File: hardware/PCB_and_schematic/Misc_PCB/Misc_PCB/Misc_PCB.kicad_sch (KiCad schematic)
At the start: 0 parts

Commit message: add misc board schematic
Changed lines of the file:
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@@
 	)
 	(sheet
-		(at 18.796 59.944)
-		(size 55.626 36.576)
+		(at 18.796 64.389)
+		(size 44.069 27.686)
 		(fields_autoplaced yes)
 		(stroke
@@
 		)
 		(property "Sheetname" "SD Card Switcher"
-			(at 18.796 59.2324 0)
+			(at 18.796 63.3124 0)
 			(effects
 				(font
-					(size 1.27 1.27)
+					(size 2 2)
+					(bold yes)
 				)
 				(justify left bottom)
@@
 		)
 		(property "Sheetfile" "schematics/sd_card_switcher_sch.kicad_sch"
-			(at 18.796 97.1046 0)
+			(at 18.796 92.6596 0)
 			(effects
 				(font

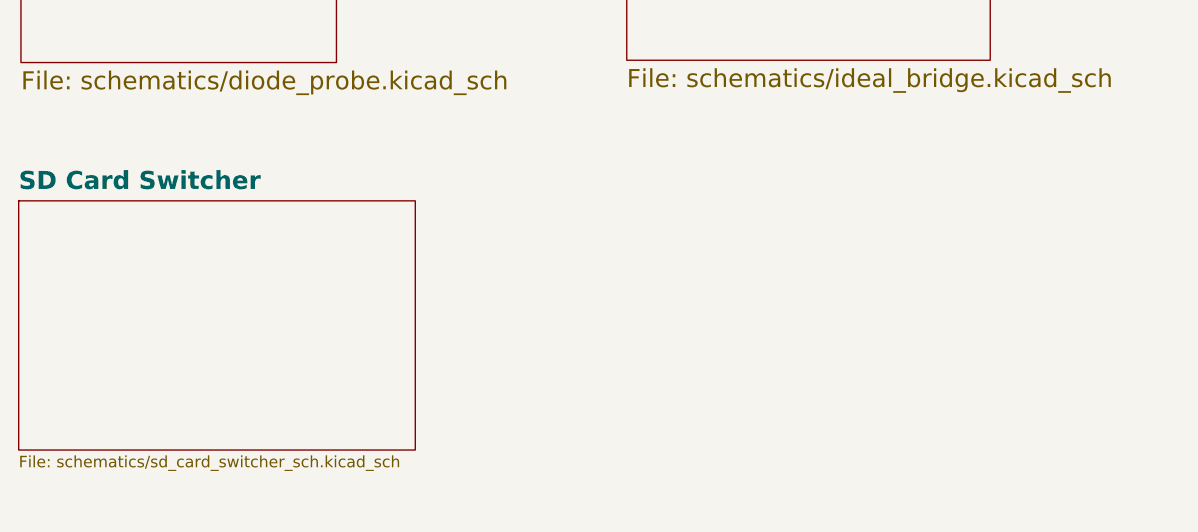
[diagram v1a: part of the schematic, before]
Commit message: Add SD card switcher circuit, some changes in pcb and schematic
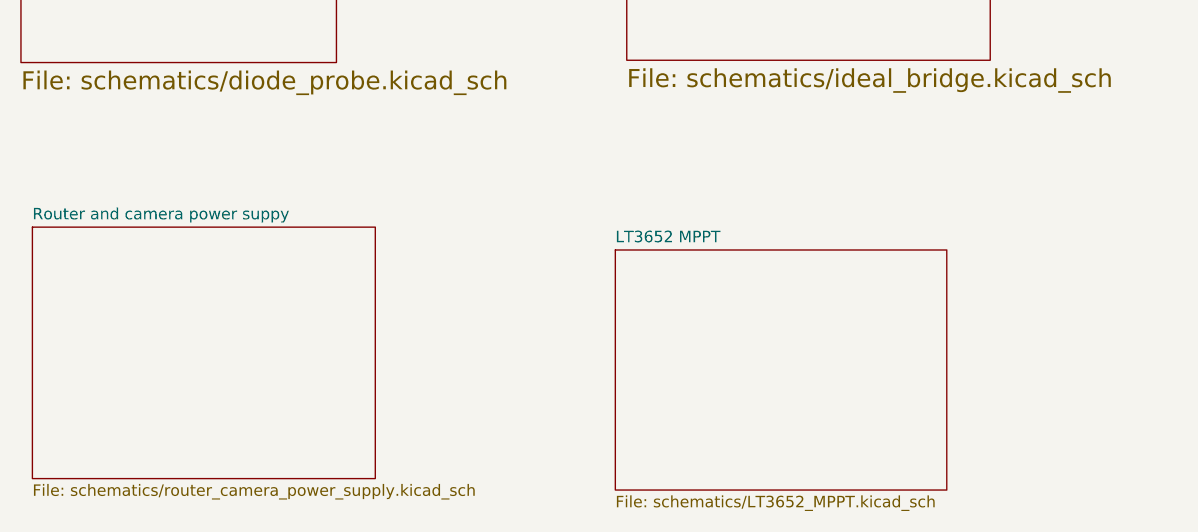
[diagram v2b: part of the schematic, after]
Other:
- removed sheet SD Card Switcher
- added sheet LT3652 MPPT (schematics/LT3652_MPPT.kicad_sch)
- added sheet Router and camera power suppy (schematics/router_camera_power_supply.kicad_sch)
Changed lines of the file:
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@@
 	(paper "A4")
+	(sheet
+		(at 20.32 67.31)
+		(size 38.1 27.94)
+		(fields_autoplaced yes)
+		(stroke
+			(width 0.1524)
+			(type solid)
+		)
+		(fill
+			(color 0 0 0 0.0000)
+		)
+		(property "Sheetname" "Router and camera power suppy"
+			(at 20.32 66.5984 0)
+			(effects
+				(font
+					(size 1.27 1.27)
+				)
+				(justify left bottom)
+			)
+		)
+		(property "Sheetfile" "schematics/router_camera_power_supply.kicad_sch"
+			(at 20.32 95.8346 0)
+			(effects
+				(font
+					(size 1.27 1.27)
+				)
+				(justify left top)
+			)
+		)
+		(instances
+			(project "Misc_PCB"
+				(path "/7b59bc46-701c-4caa-9db8-f0eec290561d"
+					(page "5")
+				)
+			)
+		)
+	)
+	(sheet
+		(at 85.09 69.85)
+		(size 36.83 26.67)
+		(fields_autoplaced yes)
+		(stroke
+			(width 0.1524)
+			(type solid)
+		)
+		(fill
+			(color 0 0 0 0.0000)
+		)
+		(property "Sheetname" "LT3652 MPPT"
+			(at 85.09 69.1384 0)
+			(effects
+				(font
+					(size 1.27 1.27)
+				)
+				(justify left bottom)
+			)
+		)
+		(property "Sheetfile" "schematics/LT3652_MPPT.kicad_sch"
+			(at 85.09 97.1046 0)
+			(effects
+				(font
+					(size 1.27 1.27)
+				)
+				(justify left top)
+			)
+		)
+		(instances
+			(project "Misc_PCB"
+				(path "/7b59bc46-701c-4caa-9db8-f0eec290561d"
+					(page "6")
+				)
+			)
+		)
+	)
 	(sheet
 		(at 86.36 26.67)
@@
 				)
 			)
-		)
-	)
-	(sheet
-		(at 18.796 64.389)
-		(size 44.069 27.686)
-		(fields_autoplaced yes)
-		(stroke
-			(width 0.1524)
-			(type solid)
-		)
-		(fill
-			(color 0 0 0 0.0000)
-		)
-		(property "Sheetname" "SD Card Switcher"
-			(at 18.796 63.3124 0)
-			(effects
-				(font
-					(size 2 2)
-					(bold yes)
-				)
-				(justify left bottom)
-			)
-		)
-		(property "Sheetfile" "schematics/sd_card_switcher_sch.kicad_sch"
-			(at 18.796 92.6596 0)
-			(effects
-				(font
-					(size 1.27 1.27)
-				)
-				(justify left top)
-			)
-		)
-		(instances
-			(project "Misc_PCB"
-				(path "/7b59bc46-701c-4caa-9db8-f0eec290561d"
-					(page "5")
-				)
-			)

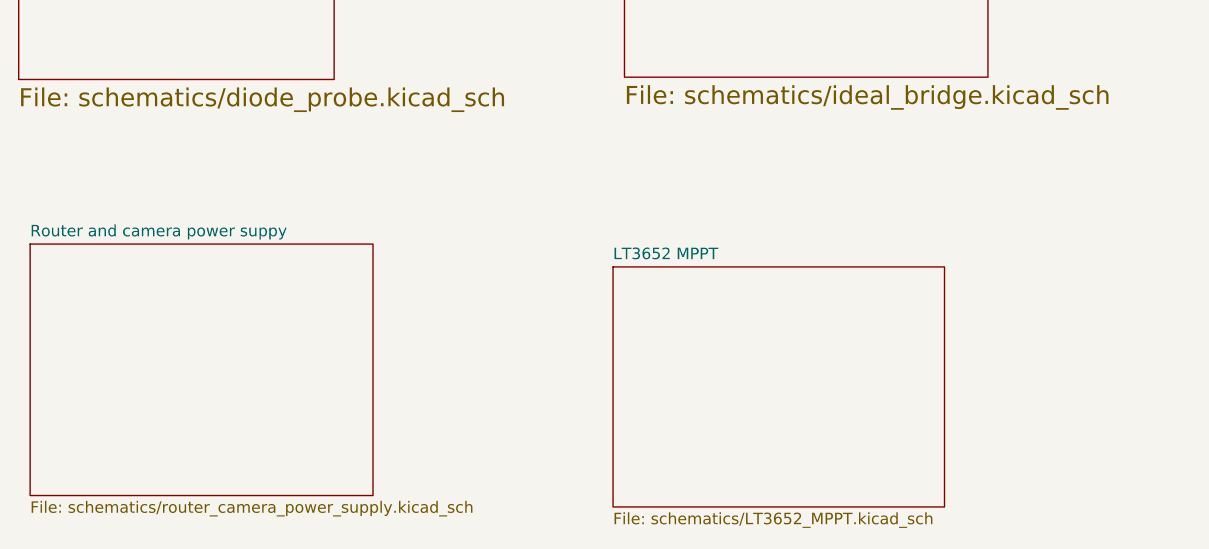
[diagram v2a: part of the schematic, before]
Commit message: add power tracking heater
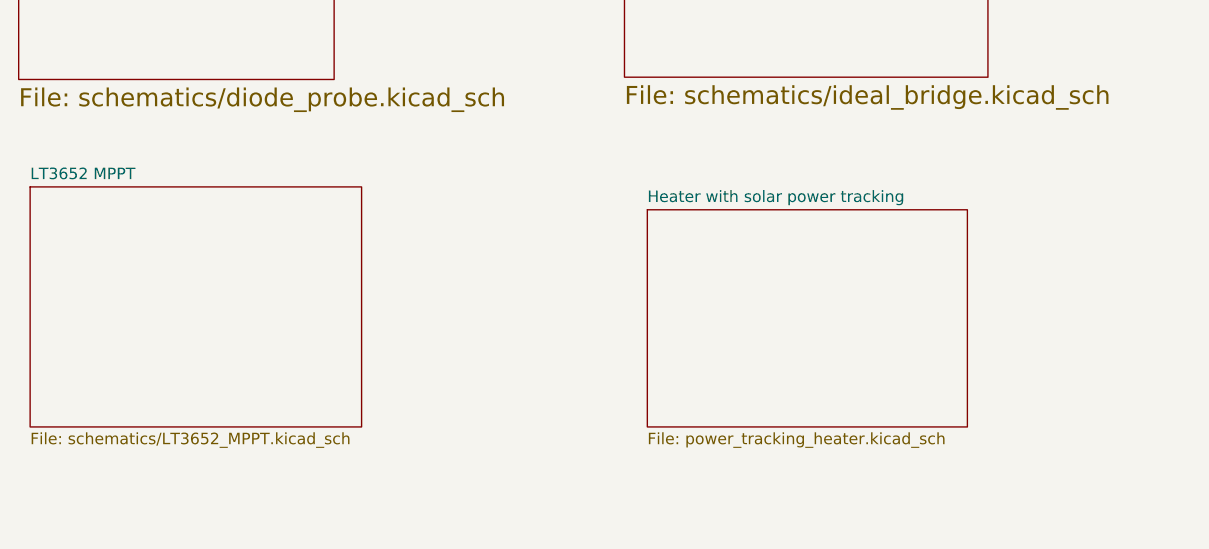
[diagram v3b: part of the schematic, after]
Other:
- removed sheet Router and camera power suppy
- added sheet Heater with solar power tracking (power_tracking_heater.kicad_sch)
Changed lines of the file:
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@@
 	(paper "A4")
 	(sheet
-		(at 20.32 67.31)
-		(size 38.1 27.94)
+		(at 88.9 63.5)
+		(size 35.56 24.13)
 		(fields_autoplaced yes)
 		(stroke
@@
 			(color 0 0 0 0.0000)
 		)
-		(property "Sheetname" "Router and camera power suppy"
-			(at 20.32 66.5984 0)
+		(property "Sheetname" "Heater with solar power tracking"
+			(at 88.9 62.7884 0)
 			(effects
 				(font
@@
 			)
 		)
-		(property "Sheetfile" "schematics/router_camera_power_supply.kicad_sch"
-			(at 20.32 95.8346 0)
+		(property "Sheetfile" "power_tracking_heater.kicad_sch"
+			(at 88.9 88.2146 0)
 			(effects
 				(font
@@
 			(project "Misc_PCB"
 				(path "/7b59bc46-701c-4caa-9db8-f0eec290561d"
-					(page "5")
+					(page "6")
 				)
 			)
@@
 	)
 	(sheet
-		(at 85.09 69.85)
+		(at 20.32 60.96)
 		(size 36.83 26.67)
 		(fields_autoplaced yes)
@@
 		)
 		(property "Sheetname" "LT3652 MPPT"
-			(at 85.09 69.1384 0)
+			(at 20.32 60.2484 0)
 			(effects
 				(font
@@
 		)
 		(property "Sheetfile" "schematics/LT3652_MPPT.kicad_sch"
-			(at 85.09 97.1046 0)
+			(at 20.32 88.2146 0)
 			(effects
 				(font

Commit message: progress with esp power pcb
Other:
- sheet Shift Register for LCD Display renamed Shift Register for 40x4 LCD Display
- added sheet Shift Register for 16x2 LCD Display (schematics/shift_register_display_2x16.kicad_sch)
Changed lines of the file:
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@@
 	(paper "A4")
 	(sheet
-		(at 88.9 63.5)
+		(at 82.55 63.5)
 		(size 35.56 24.13)
 		(fields_autoplaced yes)
@@
 		)
 		(property "Sheetname" "Heater with solar power tracking"
-			(at 88.9 62.7884 0)
-			(effects
-				(font
-					(size 1.27 1.27)
+			(at 82.55 62.1734 0)
+			(effects
+				(font
+					(size 2.5 2.5)
+					(bold yes)
 				)
 				(justify left bottom)
@@
 		)
 		(property "Sheetfile" "power_tracking_heater.kicad_sch"
-			(at 88.9 88.2146 0)
+			(at 82.55 88.2146 0)
 			(effects
 				(font
@@
 	)
 	(sheet
-		(at 86.36 26.67)
+		(at 152.4 63.5)
+		(size 38.1 24.13)
+		(fields_autoplaced yes)
+		(stroke
+			(width 0.1524)
+			(type solid)
+		)
+		(fill
+			(color 0 0 0 0.0000)
+		)
+		(property "Sheetname" "Shift Register for 16x2 LCD Display"
+			(at 152.4 62.1734 0)
+			(effects
+				(font
+					(size 2.5 2.5)
+					(bold yes)
+				)
+				(justify left bottom)
+			)
+		)
+		(property "Sheetfile" "schematics/shift_register_display_2x16.kicad_sch"
+			(at 152.4 88.5066 0)
+			(effects
+				(font
+					(size 2 2)
+				)
+				(justify left top)
+			)
+		)
+		(instances
+			(project "Misc_PCB"
+				(path "/7b59bc46-701c-4caa-9db8-f0eec290561d"
+					(page "7")
+				)
+			)
+		)
+	)
+	(sheet
+		(at 82.55 26.67)
 		(size 40.386 22.098)
-		(fields_autoplaced yes)
 		(stroke
 			(width 0.1524)
@@
 		)
 		(property "Sheetname" "Ideal Bridge"
-			(at 86.36 25.3434 0)
+			(at 81.788 25.4 0)
 			(effects
 				(font
@@
 		)
 		(property "Sheetfile" "schematics/ideal_bridge.kicad_sch"
-			(at 86.36 49.6446 0)
+			(at 82.55 49.6446 0)
 			(effects
 				(font
@@
 		(at 19.05 26.416)
 		(size 35.052 22.606)
-		(fields_autoplaced yes)
 		(stroke
 			(width 0.1524)
@@
 		)
 		(property "Sheetname" "Diode Probe for Gamma Meter"
-			(at 19.05 25.0894 0)
+			(at 18.542 25.146 0)
 			(effects
 				(font
@@
 		(at 153.162 27.432)
 		(size 37.592 22.098)
-		(fields_autoplaced yes)
-		(stroke
-			(width 0.1524)
-			(type solid)
-		)
-		(fill
-			(color 0 0 0 0.0000)
-		)
-		(property "Sheetname" "Shift Register for LCD Display"
-			(at 153.162 26.1054 0)
-			(effects
-				(font
+		(stroke
+			(width 0.1524)
+			(type solid)
+		)
+		(fill
+			(color 0 0 0 0.0000)
+		)
+		(property "Sheetname" "Shift Register for 40x4 LCD Display"
+			(at 152.4 26.162 0)
+			(effects
+				(font

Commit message: power tracking heater progress
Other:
- removed sheet Heater with solar power tracking
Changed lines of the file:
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@@
 	(paper "A4")
-	(sheet
-		(at 82.55 63.5)
-		(size 35.56 24.13)
-		(fields_autoplaced yes)
-		(stroke
-			(width 0.1524)
-			(type solid)
-		)
-		(fill
-			(color 0 0 0 0.0000)
-		)
-		(property "Sheetname" "Heater with solar power tracking"
-			(at 82.55 62.1734 0)
-			(effects
-				(font
-					(size 2.5 2.5)
-					(bold yes)
-				)
-				(justify left bottom)
-			)
-		)
-		(property "Sheetfile" "power_tracking_heater.kicad_sch"
-			(at 82.55 88.2146 0)
-			(effects
-				(font
-					(size 1.27 1.27)
-				)
-				(justify left top)
-			)
-		)
-		(instances
-			(project "Misc_PCB"
-				(path "/7b59bc46-701c-4caa-9db8-f0eec290561d"
-					(page "6")
-				)
-			)
-		)
-	)
 	(sheet
 		(at 20.32 60.96)
